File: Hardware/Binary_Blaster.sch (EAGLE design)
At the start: 26 parts

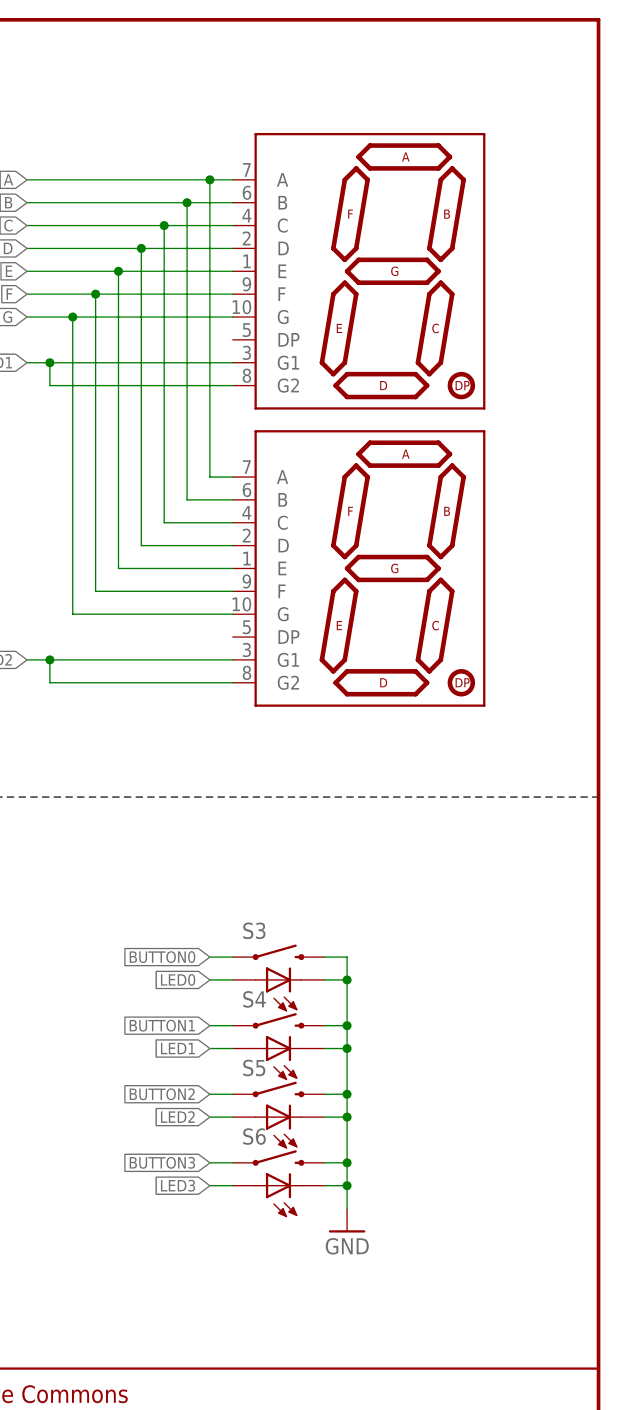
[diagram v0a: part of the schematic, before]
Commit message: Firmware and "v02" of hardware
v02: changed to "EZ" packages on display and leds, corrected silk on led
package. Moved to larger display (the we carry in house).
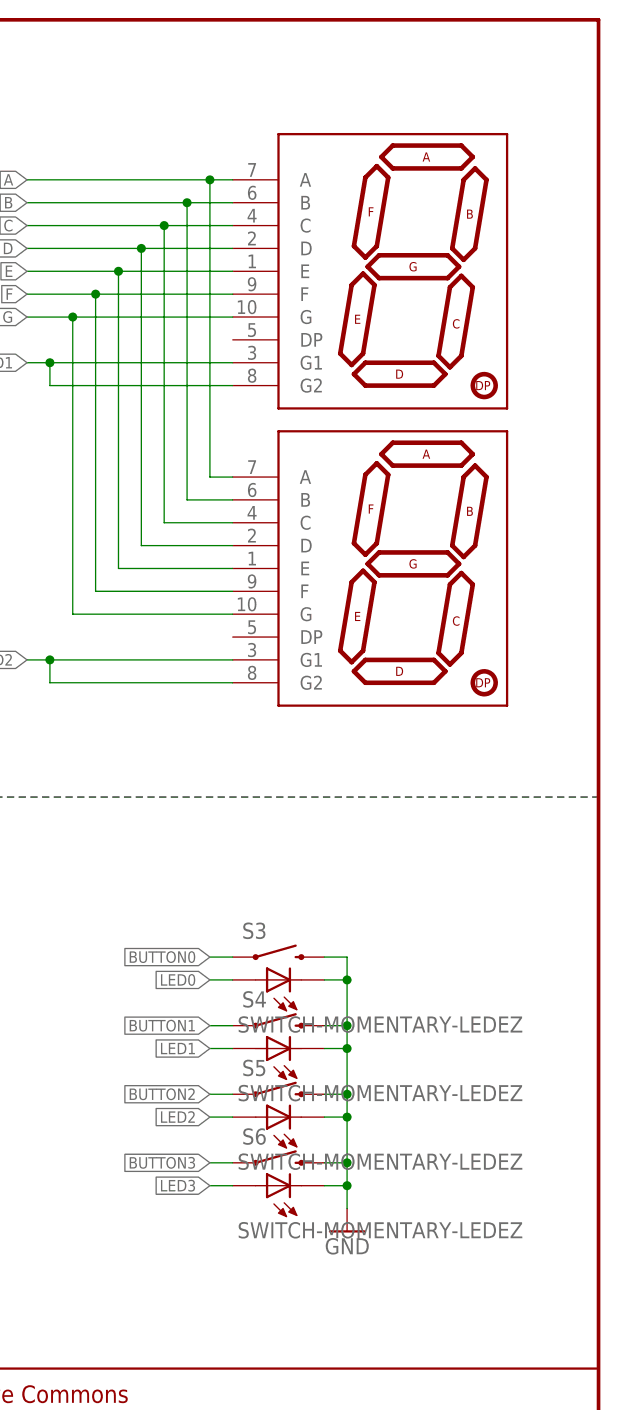
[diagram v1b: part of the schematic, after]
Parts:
- removed U$4, U$5: 7-SEGMENT-DISPLAYPTH, SparkFun-Displays:7-SEGMENT-DISPLAYPTH
- added U$1, U$6: 7-SEGMENT-DISPLAY-1"-REDEZ, SparkFun-Displays:7-SEGMENT-DISPLAY-1"-REDEZ
- S3, S4, S5, S6: value SWITCH-MOMENTARY-LEDPTH -> SWITCH-MOMENTARY-LEDEZ; device SparkFun-Electromechanical:SWITCH-MOMENTARY-LEDPTH -> SparkFun-Electromechanical:SWITCH-MOMENTARY-LEDEZ
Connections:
- net A: now also U$1.A, U$6.A; no longer U$4.A, U$5.A
- net B: now also U$1.B, U$6.B; no longer U$4.B, U$5.B
- net C: now also U$1.C, U$6.C; no longer U$4.C, U$5.C
- net D: now also U$1.D, U$6.D; no longer U$4.D, U$5.D
- net D1: now also U$1.G1, U$1.G2; no longer U$5.G1, U$5.G2
- net D2: now also U$6.G1, U$6.G2; no longer U$4.G1, U$4.G2
- net E: now also U$1.E, U$6.E; no longer U$4.E, U$5.E
- net F: now also U$1.F, U$6.F; no longer U$4.F, U$5.F
- net G: now also U$1.G, U$6.G; no longer U$4.G, U$5.G
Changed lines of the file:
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@@
 <?xml version="1.0" encoding="utf-8"?>
 <!DOCTYPE eagle SYSTEM "eagle.dtd">
-<eagle version="6.4">
+<eagle version="6.5.0">
 <drawing>
 <settings>
@@
 <layer number="19" name="Unrouted" color="11" fill="1" visible="no" active="no"/>
 <layer number="20" name="Dimension" color="15" fill="1" visible="no" active="no"/>
-<layer number="21" name="tPlace" color="16" fill="1" visible="no" active="no"/>
+<layer number="21" name="tPlace" color="15" fill="1" visible="no" active="no"/>
 <layer number="22" name="bPlace" color="14" fill="1" visible="no" active="no"/>
 <layer number="23" name="tOrigins" color="15" fill="1" visible="no" active="no"/>
@@
 <part name="P+9" library="SparkFun" deviceset="3.3V" device=""/>
 <part name="GND1" library="SparkFun" deviceset="GND" device=""/>
-<part name="U$4" library="SparkFun-Displays" deviceset="7-SEGMENT-DISPLAY" device="PTH" value=""/>
-<part name="U$5" library="SparkFun-Displays" deviceset="7-SEGMENT-DISPLAY" device="PTH" value=""/>
-<part name="S3" library="SparkFun-Electromechanical" deviceset="SWITCH-MOMENTARY-LED" device="PTH" value=""/>
-<part name="S4" library="SparkFun-Electromechanical" deviceset="SWITCH-MOMENTARY-LED" device="PTH" value=""/>
-<part name="S5" library="SparkFun-Electromechanical" deviceset="SWITCH-MOMENTARY-LED" device="PTH" value=""/>
-<part name="S6" library="SparkFun-Electromechanical" deviceset="SWITCH-MOMENTARY-LED" device="PTH" value=""/>
+<part name="S3" library="SparkFun-Electromechanical" deviceset="SWITCH-MOMENTARY-LED" device="EZ" value="SWITCH-MOMENTARY-LEDEZ"/>
+<part name="S4" library="SparkFun-Electromechanical" deviceset="SWITCH-MOMENTARY-LED" device="EZ" value="SWITCH-MOMENTARY-LEDEZ"/>
+<part name="S5" library="SparkFun-Electromechanical" deviceset="SWITCH-MOMENTARY-LED" device="EZ" value="SWITCH-MOMENTARY-LEDEZ"/>
+<part name="S6" library="SparkFun-Electromechanical" deviceset="SWITCH-MOMENTARY-LED" device="EZ" value="SWITCH-MOMENTARY-LEDEZ"/>
 <part name="GND3" library="SparkFun" deviceset="GND" device=""/>
-<part name="LOGO1" library="SparkFun-Aesthetics" deviceset="LOGO-SFE" device="NEW"/>
+<part name="LOGO1" library="SparkFun-Aesthetics" deviceset="LOGO-SFE" device="NEW" value="LOGO-SFENEW"/>
 <part name="LOGO2" library="SparkFun-Aesthetics" deviceset="LOGO-SFE" device="NEW"/>
 <part name="U$2" library="SparkFun" deviceset="OSHW-LOGO" device="L" value="OSHW-LOGOL"/>
+<part name="U$1" library="SparkFun-Displays" deviceset="7-SEGMENT-DISPLAY-1&quot;-RED" device="EZ" value="7-SEGMENT-DISPLAY-1&quot;-REDEZ"/>
+<part name="U$6" library="SparkFun-Displays" deviceset="7-SEGMENT-DISPLAY-1&quot;-RED" device="EZ" value="7-SEGMENT-DISPLAY-1&quot;-REDEZ"/>
 </parts>
 <sheets>
@@
 <instance part="P+9" gate="G$1" x="73.66" y="127"/>
 <instance part="GND1" gate="1" x="220.98" y="50.8" rot="MR0"/>
-<instance part="U$4" gate="G$1" x="226.06" y="124.46"/>
-<instance part="U$5" gate="G$1" x="226.06" y="157.48"/>
 <instance part="S3" gate="G$1" x="213.36" y="81.28"/>
 <instance part="S4" gate="G$1" x="213.36" y="73.66"/>
@@
 <instance part="LOGO2" gate="G$1" x="83.82" y="5.08"/>
 <instance part="U$2" gate="G$1" x="106.68" y="12.7"/>
+<instance part="U$1" gate="G$1" x="228.6" y="157.48"/>
+<instance part="U$6" gate="G$1" x="228.6" y="124.46"/>
 </instances>
 <busses>
@@
 <net name="A" class="0">
 <segment>
-<pinref part="U$4" gate="G$1" pin="A"/>
-<pinref part="U$5" gate="G$1" pin="A"/>
 <wire x1="208.28" y1="167.64" x2="205.74" y2="167.64" width="0.1524" layer="91"/>
 <wire x1="205.74" y1="167.64" x2="205.74" y2="134.62" width="0.1524" layer="91"/>
@@
 <junction x="205.74" y="167.64"/>
 <label x="185.42" y="167.64" size="1.27" layer="95" rot="R180" xref="yes"/>
+<pinref part="U$1" gate="G$1" pin="A"/>
+<pinref part="U$6" gate="G$1" pin="A"/>
 </segment>
 <segment>
@@
 <net name="B" class="0">
 <segment>
-<pinref part="U$4" gate="G$1" pin="B"/>
-<pinref part="U$5" gate="G$1" pin="B"/>
 <wire x1="208.28" y1="165.1" x2="203.2" y2="165.1" width="0.1524" layer="91"/>
 <wire x1="203.2" y1="165.1" x2="203.2" y2="132.08" width="0.1524" layer="91"/>
@@
 <junction x="203.2" y="165.1"/>
 <label x="185.42" y="165.1" size="1.27" layer="95" rot="R180" xref="yes"/>
+<pinref part="U$1" gate="G$1" pin="B"/>
+<pinref part="U$6" gate="G$1" pin="B"/>
 </segment>
 <segment>
@@
 <net name="C" class="0">
 <segment>
-<pinref part="U$4" gate="G$1" pin="C"/>
-<pinref part="U$5" gate="G$1" pin="C"/>
 <wire x1="208.28" y1="162.56" x2="200.66" y2="162.56" width="0.1524" layer="91"/>
 <wire x1="200.66" y1="162.56" x2="200.66" y2="129.54" width="0.1524" layer="91"/>
@@
 <junction x="200.66" y="162.56"/>
 <label x="185.42" y="162.56" size="1.27" layer="95" rot="R180" xref="yes"/>
+<pinref part="U$1" gate="G$1" pin="C"/>
+<pinref part="U$6" gate="G$1" pin="C"/>
 </segment>
 <segment>
@@
 <net name="D" class="0">
 <segment>
-<pinref part="U$4" gate="G$1" pin="D"/>
-<pinref part="U$5" gate="G$1" pin="D"/>
 <wire x1="208.28" y1="160.02" x2="198.12" y2="160.02" width="0.1524" layer="91"/>
 <wire x1="198.12" y1="160.02" x2="198.12" y2="127" width="0.1524" layer="91"/>
@@
 <junction x="198.12" y="160.02"/>
 <label x="185.42" y="160.02" size="1.27" layer="95" rot="R180" xref="yes"/>
+<pinref part="U$1" gate="G$1" pin="D"/>
+<pinref part="U$6" gate="G$1" pin="D"/>
 </segment>
 <segment>
@@
 <net name="E" class="0">
 <segment>
-<pinref part="U$4" gate="G$1" pin="E"/>
-<pinref part="U$5" gate="G$1" pin="E"/>
 <wire x1="208.28" y1="157.48" x2="195.58" y2="157.48" width="0.1524" layer="91"/>
 <wire x1="195.58" y1="157.48" x2="195.58" y2="124.46" width="0.1524" layer="91"/>
@@
 <junction x="195.58" y="157.48"/>
 <label x="185.42" y="157.48" size="1.27" layer="95" rot="R180" xref="yes"/>
+<pinref part="U$1" gate="G$1" pin="E"/>
+<pinref part="U$6" gate="G$1" pin="E"/>
 </segment>
 <segment>
@@
 <net name="F" class="0">
 <segment>
-<pinref part="U$4" gate="G$1" pin="F"/>
-<pinref part="U$5" gate="G$1" pin="F"/>
 <wire x1="208.28" y1="154.94" x2="193.04" y2="154.94" width="0.1524" layer="91"/>
 <wire x1="193.04" y1="154.94" x2="193.04" y2="121.92" width="0.1524" layer="91"/>
@@
 <junction x="193.04" y="154.94"/>
 <label x="185.42" y="154.94" size="1.27" layer="95" rot="R180" xref="yes"/>
+<pinref part="U$1" gate="G$1" pin="F"/>
+<pinref part="U$6" gate="G$1" pin="F"/>
 </segment>
 <segment>
@@
 <net name="G" class="0">
 <segment>
-<pinref part="U$4" gate="G$1" pin="G"/>
-<pinref part="U$5" gate="G$1" pin="G"/>
 <wire x1="208.28" y1="152.4" x2="190.5" y2="152.4" width="0.1524" layer="91"/>
 <wire x1="190.5" y1="152.4" x2="190.5" y2="119.38" width="0.1524" layer="91"/>
@@
 <junction x="190.5" y="152.4"/>
 <label x="185.42" y="152.4" size="1.27" layer="95" rot="R180" xref="yes"/>
+<pinref part="U$1" gate="G$1" pin="G"/>
+<pinref part="U$6" gate="G$1" pin="G"/>
 </segment>
 <segment>
@@
 <net name="D1" class="0">
 <segment>
-<pinref part="U$5" gate="G$1" pin="G1"/>
 <wire x1="208.28" y1="147.32" x2="187.96" y2="147.32" width="0.1524" layer="91"/>
 <label x="185.42" y="147.32" size="1.27" layer="95" rot="R180" xref="yes"/>
-<pinref part="U$5" gate="G$1" pin="G2"/>
 <wire x1="187.96" y1="147.32" x2="185.42" y2="147.32" width="0.1524" layer="91"/>
 <wire x1="208.28" y1="144.78" x2="187.96" y2="144.78" width="0.1524" layer="91"/>
 <wire x1="187.96" y1="144.78" x2="187.96" y2="147.32" width="0.1524" layer="91"/>
 <junction x="187.96" y="147.32"/>
+<pinref part="U$1" gate="G$1" pin="G1"/>
+<pinref part="U$1" gate="G$1" pin="G2"/>
 </segment>
 <segment>
@@
 <net name="D2" class="0">
 <segment>
-<pinref part="U$4" gate="G$1" pin="G1"/>
 <wire x1="208.28" y1="114.3" x2="187.96" y2="114.3" width="0.1524" layer="91"/>
 <label x="185.42" y="114.3" size="1.27" layer="95" rot="R180" xref="yes"/>
-<pinref part="U$4" gate="G$1" pin="G2"/>
 <wire x1="187.96" y1="114.3" x2="185.42" y2="114.3" width="0.1524" layer="91"/>
 <wire x1="208.28" y1="111.76" x2="187.96" y2="111.76" width="0.1524" layer="91"/>
 <wire x1="187.96" y1="111.76" x2="187.96" y2="114.3" width="0.1524" layer="91"/>
 <junction x="187.96" y="114.3"/>
-</segment>
-<segment>
+<pinref part="U$6" gate="G$1" pin="G1"/>
+<pinref part="U$6" gate="G$1" pin="G2"/>
+</segment>
+<segment>
